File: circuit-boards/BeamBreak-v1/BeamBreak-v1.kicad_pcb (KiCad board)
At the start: 2 copper layers, 53.3 x 27.9 mm, 39 parts, among them J1 Power, J2 SENSOR, J3 OUT, Q1 SI2318CDS-T1-GE3, U1 ITS41k0S-ME-N, U2 LM3478MA, U3 FODM121A

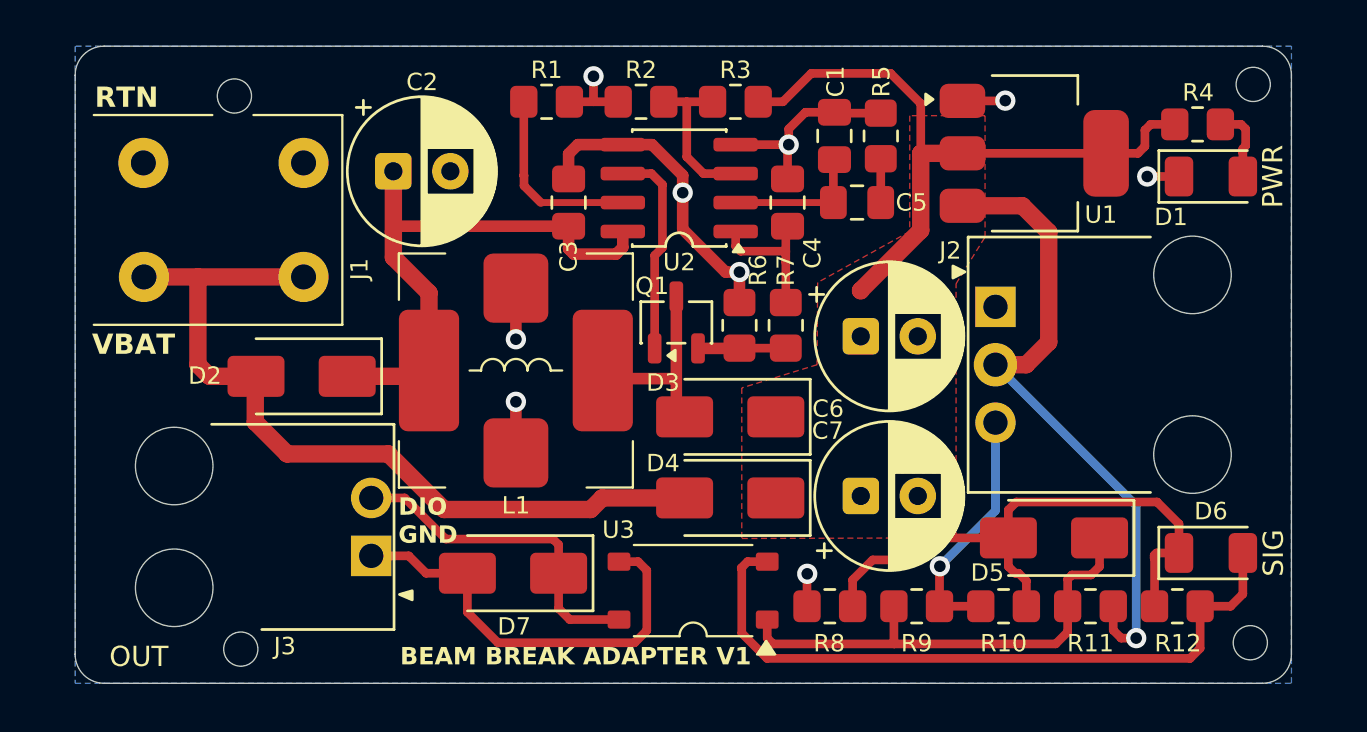
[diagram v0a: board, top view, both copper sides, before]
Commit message: Chagned opto-coupler to totem pole output to drive 5V DIO with weak pull-up
Signed-off-by: Scott Berman <sgberman1@gmail.com>
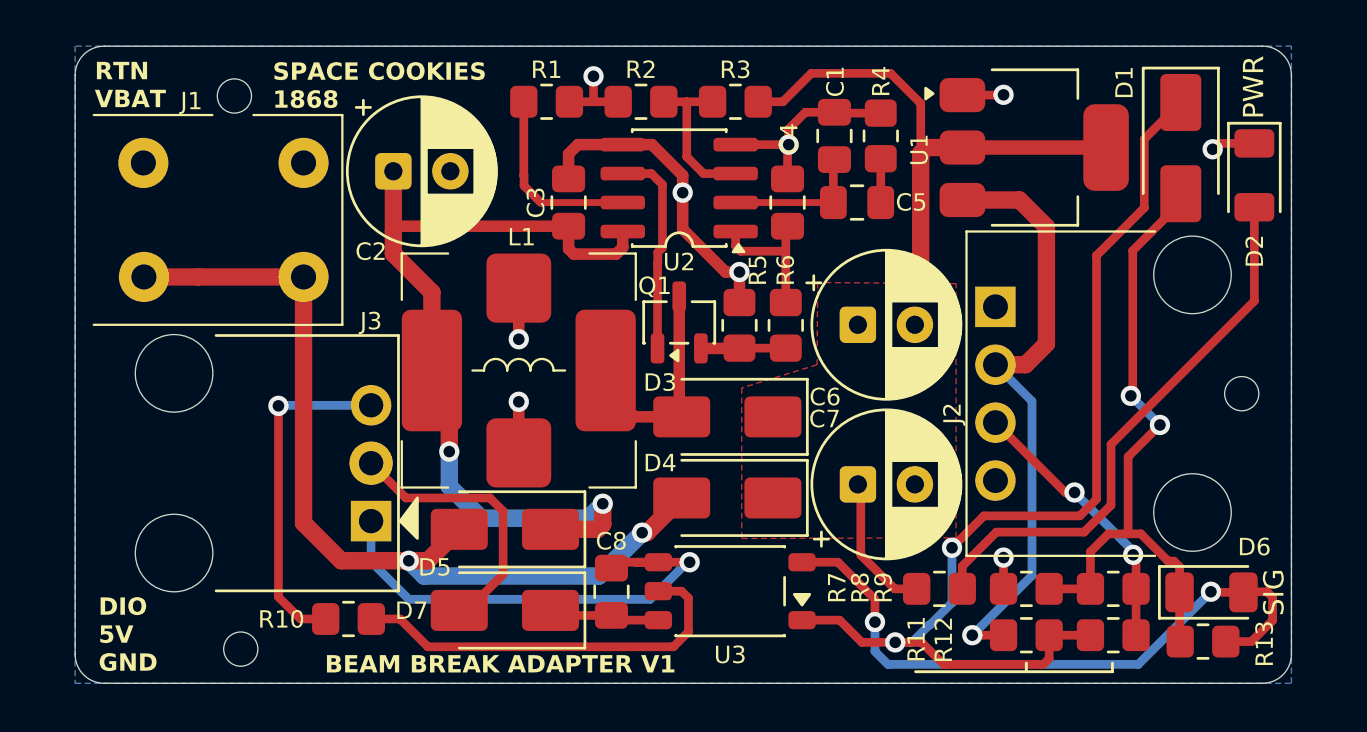
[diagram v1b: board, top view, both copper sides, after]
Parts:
- removed H1: 1.5mm Tooling Hole, BeamBreak:ToolingHole_1.5mm
- removed the H3 at (214.3, 121.9)
- added C8: 0.1uF-50V-5%-0805, Capacitor_SMD:C_0805_2012Metric_Pad1.18x1.45mm_HandSolder, F.Cu at (186.3, 119.7)
- added R10: 100R-1%-0805, Resistor_SMD:R_0805_2012Metric_Pad1.20x1.40mm_HandSolder, F.Cu at (174.8, 120.9)
- J2: footprint BeamBreak:Molex-70555-0002 -> BeamBreak:Molex-70555-0003
- J3: footprint BeamBreak:Molex-70555-0001 -> BeamBreak:Molex-70555-0002
- U3: value FODM121A -> TLP2361(TPL,E; footprint BeamBreak:onsemi-FODM121A -> Package_SO:SO-5-6_4.55x3.7mm_P1.27mm
- moved R7 23.3 mm to (200.7, 119.6)
- moved D1 18.0 mm to (211.3, 100.2), turned to -90 degrees
- moved D5 11.2 mm to (181.6, 116.9)
- moved R12 8.71 mm to (208.3, 121.6)
- moved R8 8.65 mm to (204.5, 119.6)
- moved R9 4.87 mm to (208.3, 119.6), turned to 180 degrees
- moved G1 3.89 mm to (194.3, 111.2)
- moved R11 3.08 mm to (204.5, 121.6), turned to 180 degrees
- moved J3 2.79 mm to (175.8, 114.0)
- moved J2 2.54 mm to (203.1, 112.3), turned to 90 degrees
- moved R13 1.92 mm to (212.3, 121.9)
- moved D2 1.91 mm to (214.5, 101.4), turned to -90 degrees
- moved D6 1.73 mm to (212.6, 119.7)
- moved D7 1.67 mm to (181.6, 120.5)
- moved U3 1.63 mm to (191.5, 119.7), turned to 180 degrees
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- renumbered D5 to D1, D1 to D2, D2 to D5, H4 to H3, R9 to R12, R12 to R13, R5 to R4, R6 to R5, R7 to R6, R4 to R7, R10 to R9
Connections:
- D7 pad 1: /DIO_RIO -> +5V_ISO
- D7 pad 2: /GND_RIO -> /+5V_RIO
- J3 pad 1: /GND_RIO -> GND_ISO
- J3 pad 2: /DIO_RIO -> /+5V_RIO
- U3 pad 3: /GND_RIO -> Net-(D6-A)
- U3 pad 4: /DIO_RIO -> GND_ISO
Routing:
- net Net-(D1-K): track 21.2 -> 46.4 mm, vias 0 -> 2
- net GND_ISO: track 0.00 -> 21.6 mm, vias 0 -> 1
- net Net-(D2-A): track 3.37 -> 24.3 mm
- net /GND_RIO: track 18.9 -> 0.00 mm
- net Net-(U3-VO): track 0.00 -> 17.6 mm
- net /Power Supply/DCDC_IN: track 25.0 -> 38.6 mm, vias 0 -> 2
- net /+5V_RIO: track 0.00 -> 12.0 mm
- net +5V_ISO: track 0.00 -> 4.91 mm
- net /Power Supply/DCIN: track 36.3 -> 39.9 mm, vias 0 -> 2
- net Net-(D3-A): track 8.80 -> 12.3 mm
- net Net-(D1-A): track 26.1 -> 28.9 mm, vias 0 -> 2
- net Net-(D6-A): track 30.6 -> 28.7 mm, vias 0 -> 2
- net +12V: track 28.6 -> 26.9 mm
- net /SIG: track 10.9 -> 12.1 mm, vias 1 -> 2
- net Net-(D3-K): track 29.7 -> 30.9 mm
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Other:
- board text added: "DIO 5V GND"
- board text added: "OUTPUT 1 GND 2 +5V 3 DIO"
- board text added: "RTN VBAT"
- board text added: "SENSOR 1 GND 2 12V 3 SIG 4 NC"
- board text added: "SPACE COOKIES 1868"
- board text removed: "DIO GND"
- board text removed: "OUTPUT 1 GND 2 DIO"
- board text removed: "RTN"
- board text removed: "SENSOR 1 GND 2 12V 3 SIG"
- board text removed: "VBAT"

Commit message: Improved placement and routing
Signed-off-by: Scott Berman <sgberman1@gmail.com>
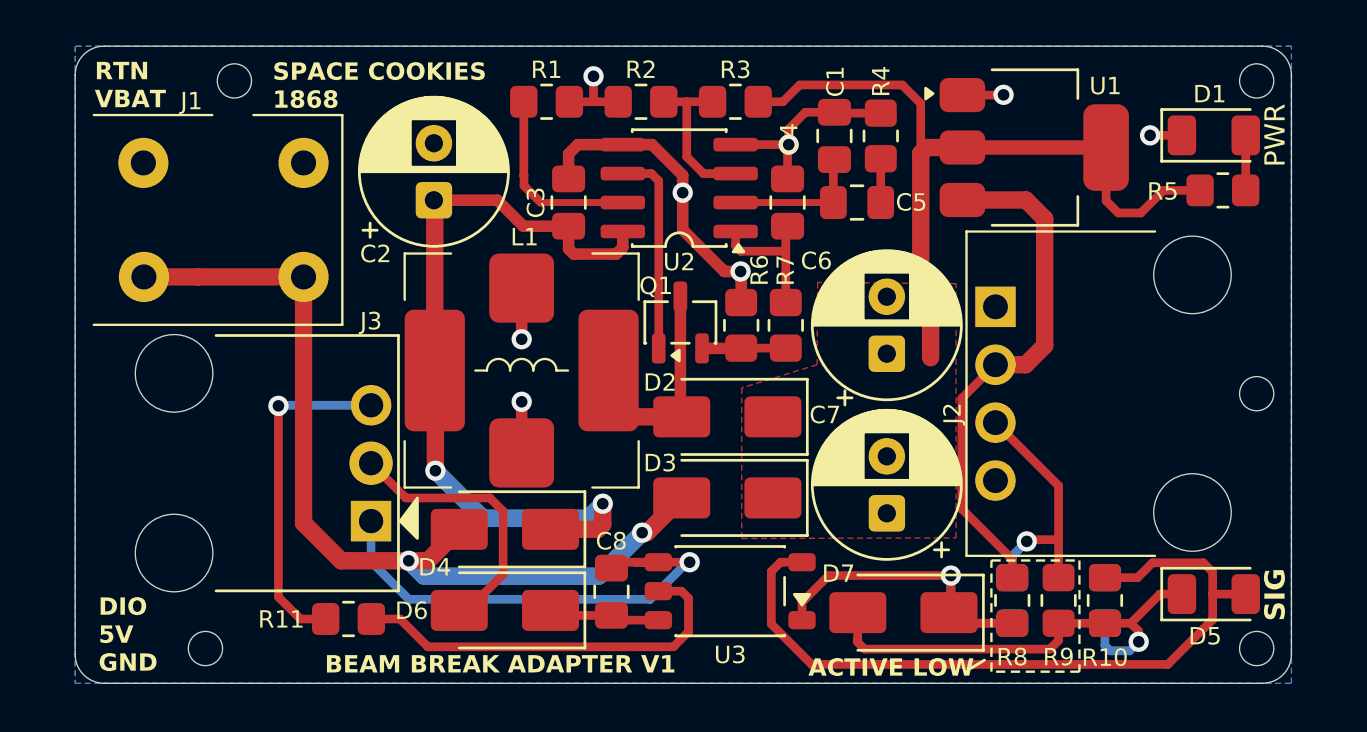
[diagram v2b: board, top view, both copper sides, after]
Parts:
- added H1: 1.5mm Tooling Hole, BeamBreak:ToolingHole_1.5mm, F.Cu at (214.6, 97.3)
- added H4: 1.5mm Tooling Hole, BeamBreak:ToolingHole_1.5mm, F.Cu at (214.6, 122.2)
- R12: renamed from R8; moved to B.Cu
- R13: renamed from R12; moved to B.Cu
- moved D7 23.7 mm to (199.1, 120.6), turned to 180 degrees
- moved R5 21.4 mm to (213.1, 102.1)
- moved R13 4.68 mm to (203.9, 120.1), turned to -90 degrees
- moved R10 4.66 mm to (207.9, 120.1), turned to 90 degrees
- moved R12 3.48 mm to (207.9, 120.1), turned to -90 degrees
- moved D1 2.50 mm to (212.7, 99.7), turned to 0 degrees
- moved R9 2.45 mm to (205.9, 120.1), turned to -90 degrees
- moved C2 2.18 mm to (178.5, 102.5), turned to 90 degrees
- moved C6 1.80 mm to (198.4, 109.2), turned to 90 degrees
- moved C7 1.80 mm to (198.4, 116.2), turned to 90 degrees
- moved R8 1.64 mm to (203.9, 120.1), turned to 90 degrees
- moved H3 1.55 mm to (168.5, 122.2)
- moved H2 0.66 mm to (169.8, 97.3)
- moved L1 0.13 mm to (182.4, 110.0)
- moved D5 0.13 mm to (212.7, 119.8)
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- renumbered D2 to D1, D3 to D2, D4 to D3, D5 to D4, D6 to D5, D7 to D6, D1 to D7, R13 to R10, R10 to R11, R7 to R5, R5 to R6, R6 to R7, R11 to R8
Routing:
- net Net-(D7-K): track 46.4 -> 16.8 mm, vias 2 -> 1
- net Net-(D1-A): track 24.3 -> 2.42 mm
- net Net-(D5-K): track 28.9 -> 20.8 mm, vias 2 -> 1
- net Net-(D5-A): track 28.7 -> 33.4 mm, vias 2 -> 0
- net +12V: track 26.9 -> 22.9 mm, vias 1 -> 0
- net Net-(D2-K): track 30.9 -> 34.4 mm
- net /Power Supply/DCDC_IN: track 38.6 -> 35.5 mm
- net Net-(D2-A): track 12.3 -> 10.2 mm
- net GND: track 35.6 -> 33.8 mm, vias 9 -> 8
- net /SIG: track 12.1 -> 11.2 mm, vias 2 -> 1
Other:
- board text added: "ACTIVE HIGH"
- board text added: "ACTIVE LOW"

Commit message: Increased length to 2.2in
Signed-off-by: Scott Berman <sgberman1@gmail.com>
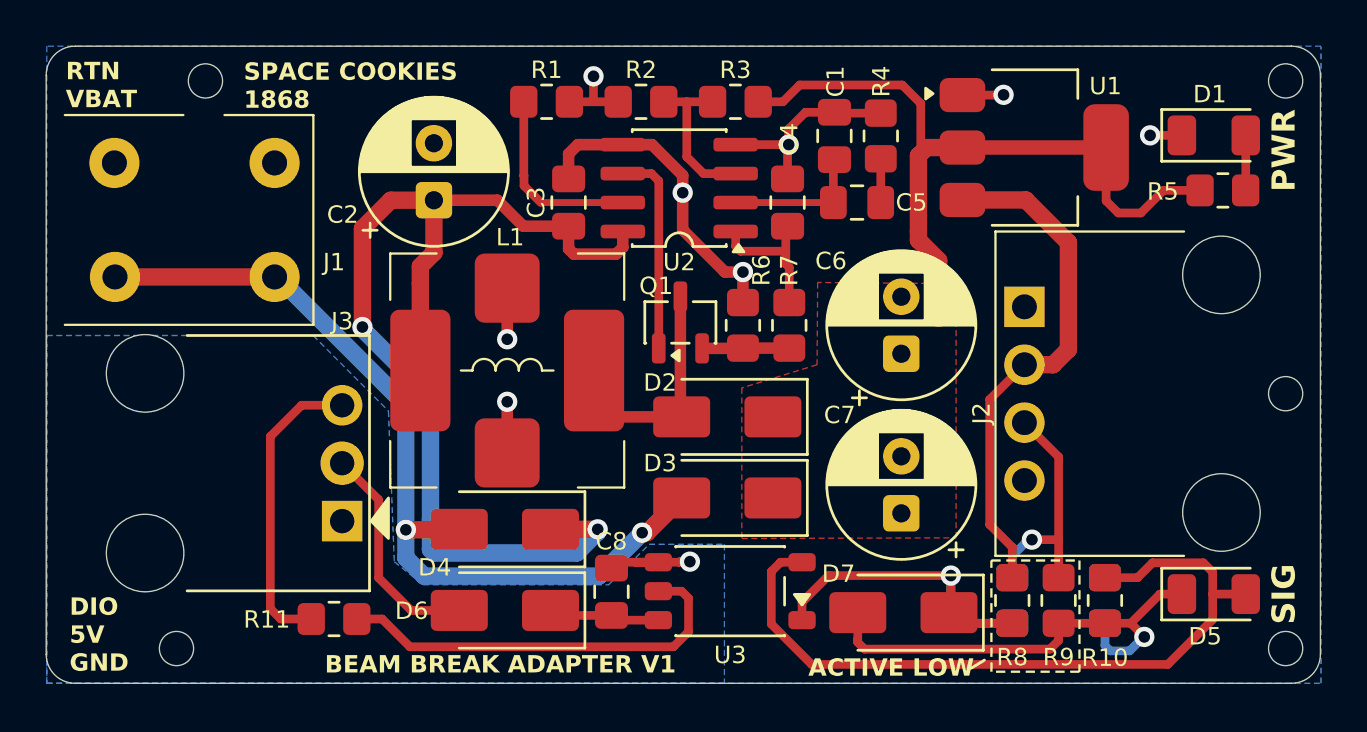
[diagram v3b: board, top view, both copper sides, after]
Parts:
- moved H3 1.27 mm to (167.2, 122.2)
- moved J1 1.27 mm to (171.5, 100.9)
- moved J3 1.27 mm to (174.5, 114.0)
- moved H1 1.27 mm to (215.9, 97.3)
- moved H2 1.27 mm to (168.5, 97.3)
- moved H4 1.27 mm to (215.9, 122.2)
- moved J2 1.27 mm to (204.4, 112.3)
- moved L1 0.64 mm to (181.7, 110.0)
- moved C6 0.63 mm to (199.0, 109.2)
- moved C7 0.63 mm to (199.0, 116.2)
- moved R11 0.63 mm to (174.1, 120.9)
- moved R7 0.15 mm to (194.1, 108.0)
- moved R6 0.08 mm to (192.1, 108.0)
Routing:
- net GND_ISO: track 21.6 -> 4.55 mm
- net /Power Supply/DCDC_IN: track 35.5 -> 48.7 mm
- net /+5V_RIO: track 12.0 -> 9.82 mm
- net Net-(D2-K): track 34.4 -> 36.3 mm
- net /DIO_RIO: track 14.9 -> 13.2 mm, vias 1 -> 0
- net /Power Supply/DCIN: track 39.9 -> 38.4 mm
- net Net-(D2-A): track 10.2 -> 11.0 mm
- net Net-(U3-VO): track 17.6 -> 18.2 mm
- net /SIG: track 11.2 -> 10.7 mm
- added copper zone on B.Cu, net GND_ISO
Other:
- board size 53.3 x 27.9 mm -> 55.9 x 27.9 mm
- board text added: "2200.00 mils x 1100.00 mils"
- board text removed: "2100.00 mils x 1100.00 mils"
